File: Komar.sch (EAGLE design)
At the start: 108 parts, among them CON1 USB-VERTICAL, CON2 PINHEAD_1X01-2, CON3 CON-4P-TABS-STRAIGHT, CON4 CON-4P-TABS-STRAIGHT, CON5 CON-4P-TABS-STRAIGHT, CON6 CON-4P-TABS-STRAIGHT, CON7 CON-4P-TABS-STRAIGHT, CON8 CON-6P-SM06B, CON9 PINHEAD_1X01-2, IC1 TPD3S014DBVR-SOT23-6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

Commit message: attribute updates
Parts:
- C1, C2: OPERATING_TEMP (none) -> -55°C ~ 105°C
- CON1: AEC-Q (none) -> ---
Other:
- moved on the sheet: CON2, CON7, CON9, D4, D7D1, D7D2, F1, PAD6, PAD7, R25, R8

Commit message: typo
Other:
- note added: "Whats new -TVS diodes replaced with ones with lower reverse standoff voltage (51 V) -Bulk capacitors replaced. The value and size increased -Overcurrent protection trip level increase 1.5x times and now is 200 A"
- note removed: "Whats new -Current shunts value increased to 1.5 mOhm -TVS diodes replaced with ones with lower reverse standoff voltage (51 V) -Bulk capacitors replaced. The value and size increased -Overcurrent protection trip level increase 1.5x times and now is 200A"
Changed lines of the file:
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@@
 <text x="27.94" y="114.3" size="1.778" layer="97">Current version 0.3</text>
 <text x="27.94" y="99.06" size="1.778" layer="97">Whats new
--Current shunts value increased to 1.5 mOhm
 -TVS diodes replaced with ones with lower reverse standoff voltage (51 V)
 -Bulk capacitors replaced. The value and size increased
--Overcurrent protection trip level increase 1.5x times and now is 200A</text>
+-Overcurrent protection trip level increase 1.5x times and now is 200 A</text>
 </plain>
 <instances>

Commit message: Update Komar.sch
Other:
- note added: "Whats new -TVS diodes replaced with ones with lower reverse standoff voltage (51 V). -Bulk capacitors replaced. The value and size increased. -Overcurrent protection trip level increase 1.5x times and now is 200 A."
- note removed: "Whats new -TVS diodes replaced with ones with lower reverse standoff voltage (51 V) -Bulk capacitors replaced. The value and size increased -Overcurrent protection trip level increase 1.5x times and now is 200 A"
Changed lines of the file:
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@@
 <text x="27.94" y="114.3" size="1.778" layer="97">Current version 0.3</text>
 <text x="27.94" y="99.06" size="1.778" layer="97">Whats new
--TVS diodes replaced with ones with lower reverse standoff voltage (51 V)
--Bulk capacitors replaced. The value and size increased
--Overcurrent protection trip level increase 1.5x times and now is 200 A</text>
+-TVS diodes replaced with ones with lower reverse standoff voltage (51 V).
+-Bulk capacitors replaced. The value and size increased.
+-Overcurrent protection trip level increase 1.5x times and now is 200 A.</text>
 </plain>
 <instances>

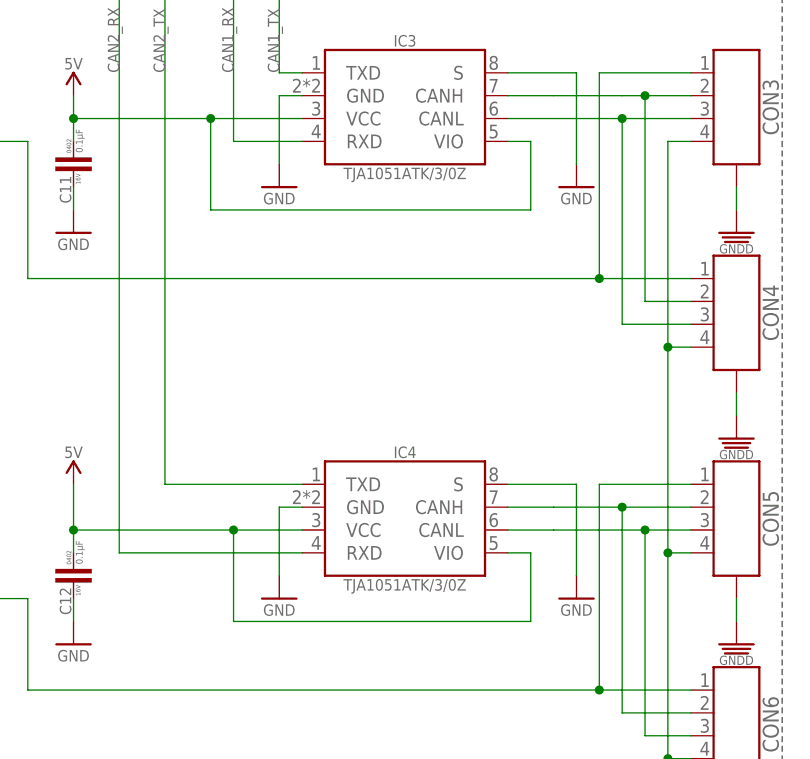
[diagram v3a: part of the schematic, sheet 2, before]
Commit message: CAN transciever replaced due for logistic reasons
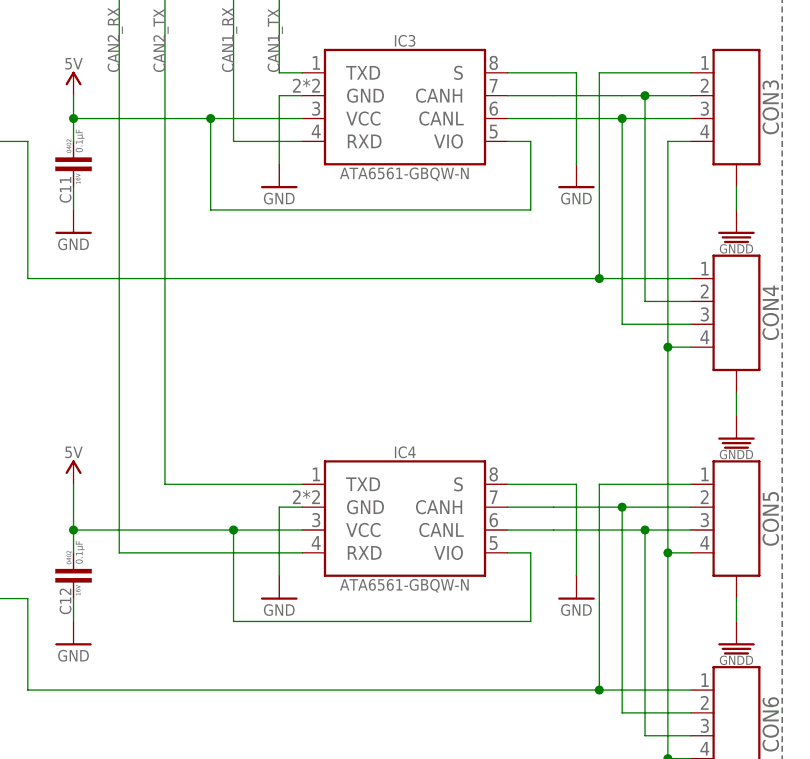
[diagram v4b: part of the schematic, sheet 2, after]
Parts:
- IC3, IC4: value TJA1051-HVSON8 -> ATA6561-GBQW-N-HVSON8; device serial_interfaces:TJA1051-HVSON8 -> serial_interfaces:ATA6561-GBQW-N-HVSON8
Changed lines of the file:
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@@
 </attributes>
 <variantdefs>
-<variantdef name="BASIC" current="yes"/>
+<variantdef name="BASIC"/>
 </variantdefs>
 <classes>
@@
 <variant name="BASIC" populate="no"/>
 </part>
-<part name="IC3" library="serial_interfaces" library_urn="urn:adsk.eagle:library:4770999" deviceset="TJA1051" device="-HVSON8" package3d_urn="urn:adsk.eagle:package:1040194/3">
+<part name="IC3" library="serial_interfaces" library_urn="urn:adsk.eagle:library:4770999" deviceset="ATA6561-GBQW-N" device="-HVSON8" package3d_urn="urn:adsk.eagle:package:1040194/3">
 <attribute name="OPERATING_TEMP" value="-40°C ~ 150°C (TJ)"/>
 </part>
@@
 <part name="GND24" library="supply_symbols" library_urn="urn:adsk.eagle:library:5017758" deviceset="GND" device="" value="GND"/>
 <part name="GND21" library="supply_symbols" library_urn="urn:adsk.eagle:library:5017758" deviceset="GND" device="" value="GND"/>
-<part name="IC4" library="serial_interfaces" library_urn="urn:adsk.eagle:library:4770999" deviceset="TJA1051" device="-HVSON8" package3d_urn="urn:adsk.eagle:package:1040194/3">
+<part name="IC4" library="serial_interfaces" library_urn="urn:adsk.eagle:library:4770999" deviceset="ATA6561-GBQW-N" device="-HVSON8" package3d_urn="urn:adsk.eagle:package:1040194/3">
 <attribute name="OPERATING_TEMP" value="-40°C ~ 150°C (TJ)"/>
 </part>

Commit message: NETs naming updates
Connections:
- net N$1 renamed BGH2
- net N$11 renamed AGL1
- net N$12 renamed CGH2
- net N$13 renamed CGL2
- net N$14 renamed CGH1
- net N$15 renamed CGL1
- net N$2 renamed BGL2
- net N$3 renamed BGL1
- net N$4 renamed BGH1
- net N$7 renamed AGH2
- net N$8 renamed AGL2
- net N$9 renamed AGH1
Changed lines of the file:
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@@
 </segment>
 </net>
-<net name="N$1" class="1">
+<net name="BGH2" class="1">
 <segment>
 <pinref part="Q1" gate="G$1" pin="G"/>
@@
 </segment>
 </net>
-<net name="N$2" class="0">
+<net name="BGL2" class="0">
 <segment>
 <pinref part="Q2" gate="G$1" pin="G"/>
@@
 </segment>
 </net>
-<net name="N$4" class="1">
+<net name="BGH1" class="1">
 <segment>
 <pinref part="Q3" gate="G$1" pin="G"/>
@@
 </segment>
 </net>
-<net name="N$3" class="0">
+<net name="BGL1" class="0">
 <segment>
 <pinref part="R4" gate="G$1" pin="2"/>
@@
 </segment>
 </net>
-<net name="N$7" class="1">
+<net name="AGH2" class="1">
 <segment>
 <pinref part="Q5" gate="G$1" pin="G"/>
@@
 </segment>
 </net>
-<net name="N$8" class="0">
+<net name="AGL2" class="0">
 <segment>
 <pinref part="Q6" gate="G$1" pin="G"/>
@@
 </segment>
 </net>
-<net name="N$9" class="1">
+<net name="AGH1" class="1">
 <segment>
 <pinref part="Q7" gate="G$1" pin="G"/>
@@
 </segment>
 </net>
-<net name="N$11" class="0">
+<net name="AGL1" class="0">
 <segment>
 <pinref part="R17" gate="G$1" pin="2"/>
@@
 </segment>
 </net>
-<net name="N$12" class="1">
+<net name="CGH2" class="1">
 <segment>
 <pinref part="Q9" gate="G$1" pin="G"/>
@@
 </segment>
 </net>
-<net name="N$13" class="0">
+<net name="CGL2" class="0">
 <segment>
 <pinref part="Q10" gate="G$1" pin="G"/>
@@
 </segment>
 </net>
-<net name="N$14" class="1">
+<net name="CGH1" class="1">
 <segment>
 <pinref part="Q11" gate="G$1" pin="G"/>
@@
 </segment>
 </net>
-<net name="N$15" class="0">
+<net name="CGL1" class="0">
 <segment>
 <pinref part="R24" gate="G$1" pin="2"/>

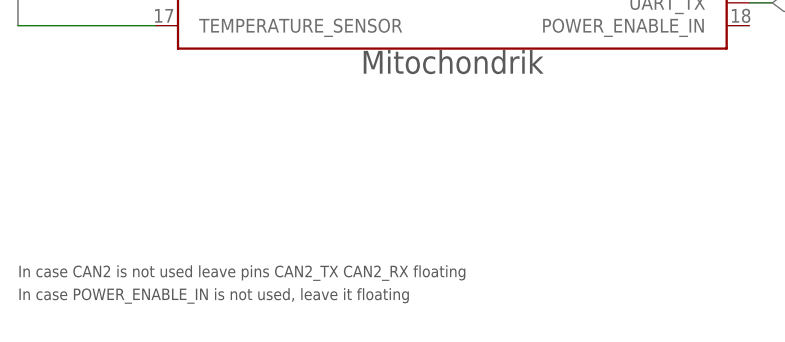
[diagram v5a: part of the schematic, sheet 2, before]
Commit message: powerstage rerouting partially completed
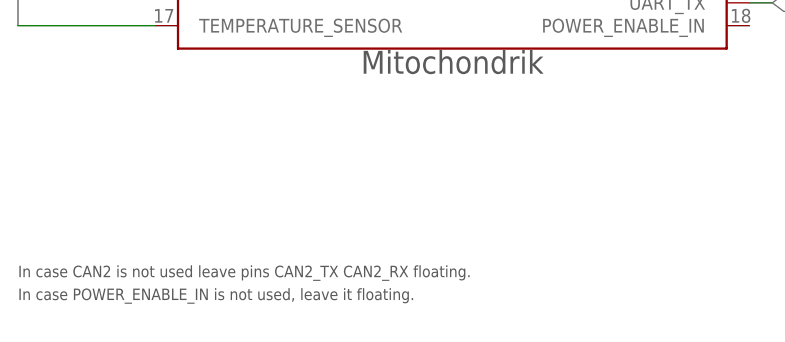
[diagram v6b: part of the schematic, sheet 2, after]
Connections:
- net BGH2 renamed JHKJ
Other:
- note added: "In case CAN2 is not used leave pins CAN2_TX CAN2_RX floating."
- note added: "In case POWER_ENABLE_IN is not used, leave it floating."
- note removed: "In case CAN2 is not used leave pins CAN2_TX CAN2_RX floating"
- note removed: "In case POWER_ENABLE_IN is not used, leave it floating"
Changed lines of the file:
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@@
 <text x="78.232" y="150.622" size="2.54" layer="97" font="vector">LOW SIDE INTERFACES</text>
 <text x="93.726" y="140.462" size="2.54" layer="97" font="vector">HIGH SIDE INTERFACES</text>
-<text x="7.62" y="12.7" size="1.27" layer="97">In case CAN2 is not used leave pins CAN2_TX CAN2_RX floating</text>
-<text x="7.62" y="10.16" size="1.27" layer="97">In case POWER_ENABLE_IN is not used, leave it floating</text>
+<text x="7.62" y="12.7" size="1.27" layer="97">In case CAN2 is not used leave pins CAN2_TX CAN2_RX floating.</text>
+<text x="7.62" y="10.16" size="1.27" layer="97">In case POWER_ENABLE_IN is not used, leave it floating.</text>
 <text x="142.24" y="160.02" size="2.54" layer="97">Place close to power mosfets</text>
 <text x="182.88" y="76.2" size="2.54" layer="97" font="vector" ratio="15" align="center">AUX</text>
@@
 </segment>
 </net>
-<net name="BGH2" class="1">
+<net name="JHKJ" class="1">
 <segment>
 <pinref part="Q1" gate="G$1" pin="G"/>

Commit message: Routing completed
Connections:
- net JHKJ renamed BGH2
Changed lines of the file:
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@@
 </segment>
 </net>
-<net name="JHKJ" class="1">
+<net name="BGH2" class="1">
 <segment>
 <pinref part="Q1" gate="G$1" pin="G"/>

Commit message: libraries cleanup
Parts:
- S1: device macaroni_masterlib:SENSE -> misc:SENSE
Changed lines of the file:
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@@
 <attribute name="OPERATING_TEMP" value="-55°C ~ 155°C"/>
 </part>
-<part name="S1" library="macaroni_masterlib" deviceset="SENSE" device="">
+<part name="S1" library="misc" library_urn="urn:adsk.eagle:library:5347860" deviceset="SENSE" device="" package3d_urn="urn:adsk.eagle:package:7365871/1">
 <variant name="BASIC" populate="no"/>
 </part>
